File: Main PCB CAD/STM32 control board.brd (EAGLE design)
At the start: 130 x 100 mm, 113 parts, among them J1 PJ-063BH, J10 S10B-PH, J11 S10B-PH, J12 S10B-PH, J13 S10B-PH, J14 S3B-PH, J15 S3B-PH, J16 S3B-PH, J17 S3B-PH, J18 DG301-4P, J2 S4B-PH, J3 S3B-PH, J4 S3B-PH, J5 S6B-PH, J8 S6B-PH, U1 TPS7A19, U10 STM32G474, U11 DRV8701VIA, U3 L2293Q, U5 REF3330, U6 REF3318, U8 ICM_20600, X1 CSTNE

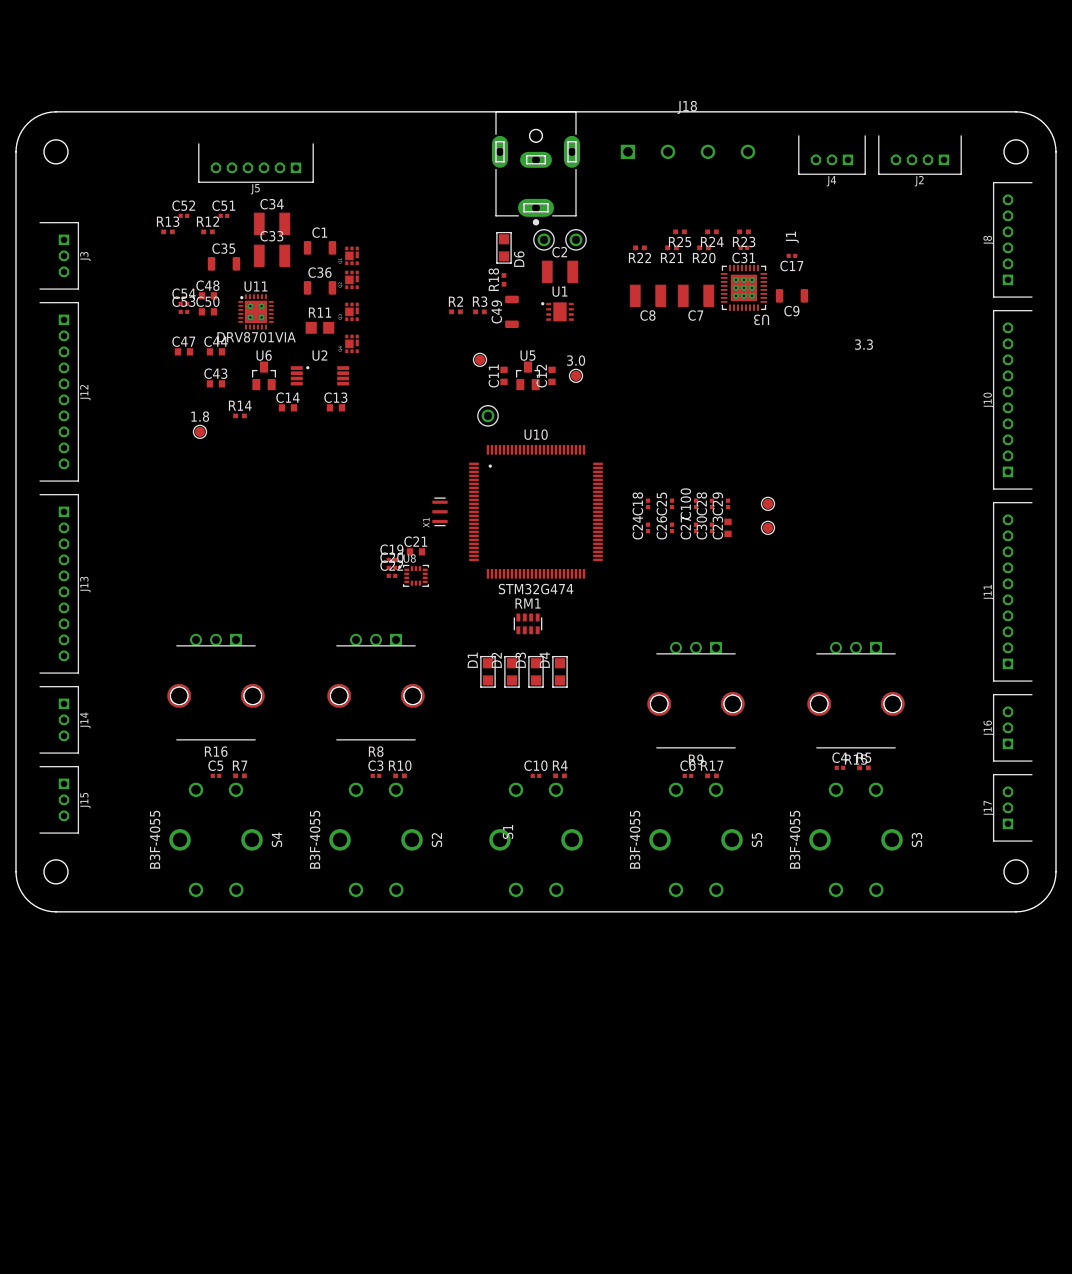
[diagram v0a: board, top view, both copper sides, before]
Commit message: renumbered schematic
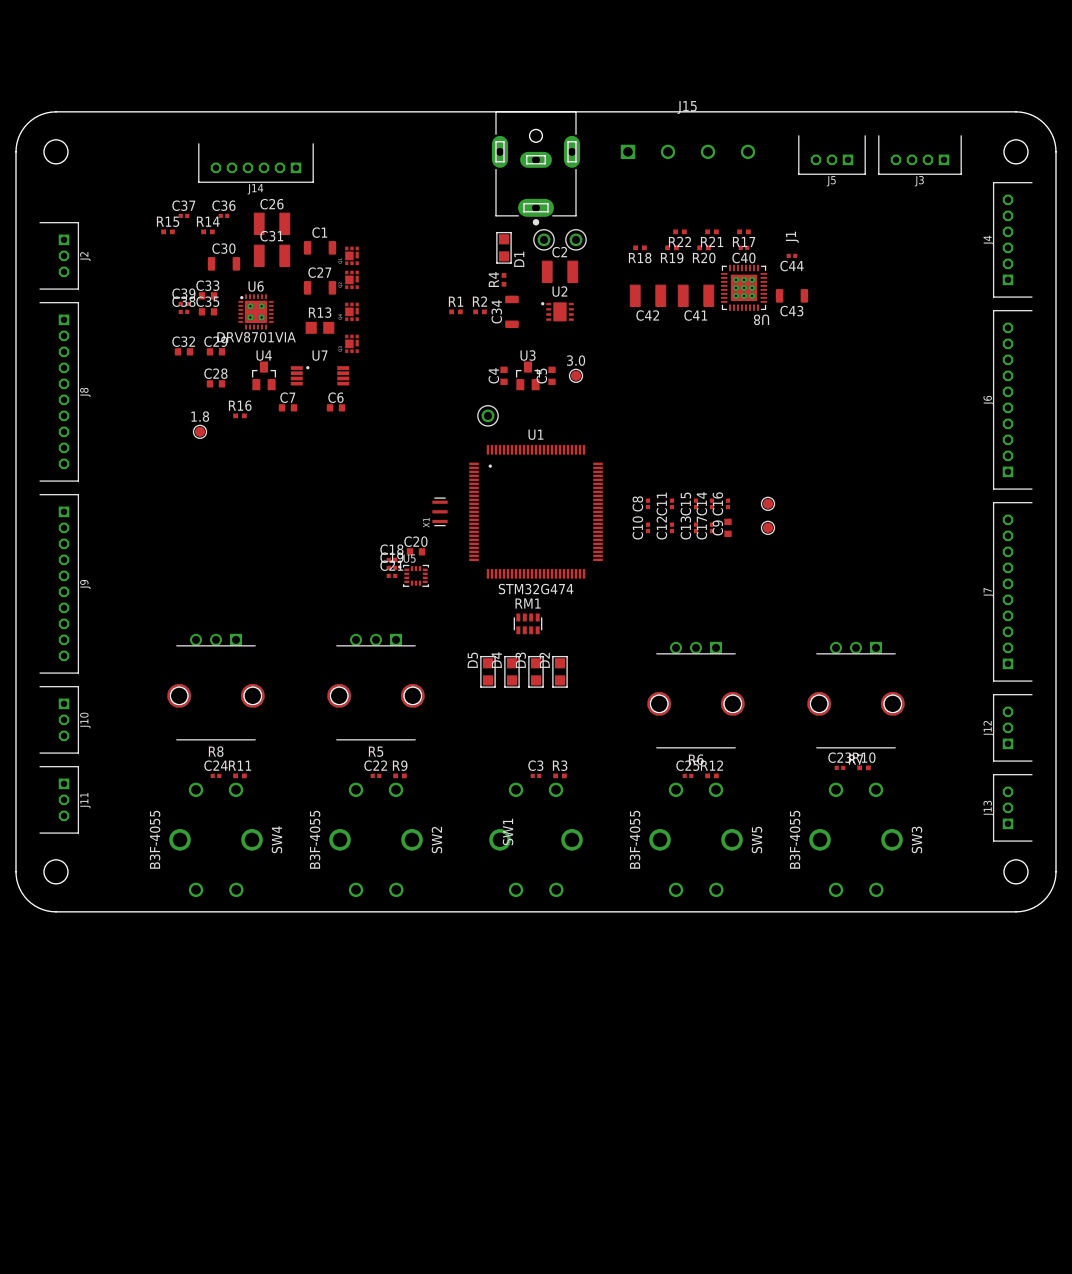
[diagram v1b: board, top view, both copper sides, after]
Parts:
- removed C48, C50: 100nF, Capacitors:C0603
- removed C49: 10uF, Capacitors:C1206
- removed C51: 1uF, Capacitors:C0402
- removed D6: Green, Semiconductor_devices:LED-0805
- removed J16, J17: S3B-PH, con-jst-ph:S3B-PH-K
- removed J18: DG301-4P, Terminal blocks:DG301-4P
- removed R23, R24, R25: 100, Resistors:R0402
- removed TP8: 3.3, testing:TP1.27MM_MASK_SILKSCREEN
- removed U10: STM32G474, stmicroelectronics:LPQFP-100
- removed U11: DRV8701VIA, Transistors drivers:VQFN-24-VIA
- added C16: 1uF, Capacitors:C0402
- added C40: 100nF, Capacitors:C0402
- added C41, C42: 47uF, Capacitors:C1210
- added D5: Blue, Semiconductor_devices:LED-0805
- added J6, J7, J9: S10B-PH, con-jst-ph:S10B-PH-K
- added R1: 16k9, Resistors:R0402
- added R19: 100, Resistors:R0402
- added R6: 10K, Resistors:ALPS_PTM
- added U4: REF3318, Voltage references:SOT-23-3
- added U7: (no value), Current sensing:TSSOP-8
- C11, C12, C13, C14, C23: value 4.7uF -> 100nF; device Capacitors:C0603 -> Capacitors:C0402
- C20, C4, C5, C6: value 100nF -> 4.7uF; device Capacitors:C0402 -> Capacitors:C0603
- C21: value 4.7uF -> 10nF; device Capacitors:C0603 -> Capacitors:C0402
- C22: value 10nF -> 100nF
- C26, C31: value 100nF -> 47uF; device Capacitors:C0402 -> Capacitors:C1210
- C27, C30: value 100nF -> 10uF; device Capacitors:C0402 -> Capacitors:C1206
- C28: device Capacitors:C0402 -> Capacitors:C0603
- C29: value 1uF -> 100nF; device Capacitors:C0402 -> Capacitors:C0603
- C33: value 47uF -> 100nF; device Capacitors:C1210 -> Capacitors:C0603
- C34: value 47uF -> 10uF; device Capacitors:C1210 -> Capacitors:C1206
- C35: value 10uF -> 100nF; device Capacitors:C1206 -> Capacitors:C0603
- C36: value 10uF -> 1uF; device Capacitors:C1206 -> Capacitors:C0402
- C43: value 100nF -> 10uF; device Capacitors:C0603 -> Capacitors:C1206
- C44: device Capacitors:C0603 -> Capacitors:C0402
- C7: value 47uF -> 4.7uF; device Capacitors:C1210 -> Capacitors:C0603
- C8: value 47uF -> 100nF; device Capacitors:C1210 -> Capacitors:C0402
- C9: value 10uF -> 4.7uF; device Capacitors:C1206 -> Capacitors:C0603
- D1: value Blue -> Green
- J10, J11, J12, J13: value S10B-PH -> S3B-PH; device con-jst-ph:S10B-PH-K -> con-jst-ph:S3B-PH-K
- J14, J4: value S3B-PH -> S6B-PH; device con-jst-ph:S3B-PH-K -> con-jst-ph:S6B-PH-K
- J15: value S3B-PH -> DG301-4P; device con-jst-ph:S3B-PH-K -> Terminal blocks:DG301-4P
- J2: value S4B-PH -> S3B-PH; device con-jst-ph:S4B-PH-K -> con-jst-ph:S3B-PH-K
- J3: value S3B-PH -> S4B-PH; device con-jst-ph:S3B-PH-K -> con-jst-ph:S4B-PH-K
- J5: value S6B-PH -> S3B-PH; device con-jst-ph:S6B-PH-K -> con-jst-ph:S3B-PH-K
- J8: value S6B-PH -> S10B-PH; device con-jst-ph:S6B-PH-K -> con-jst-ph:S10B-PH-K
- R11: value 10 mOhm -> 10k; device Resistors:CS_R0805 -> Resistors:R0402
- R13: value 10k -> 10 mOhm; device Resistors:R0402 -> Resistors:CS_R0805
- R14: value 510k -> 10k
- R15, R9: value 10K -> 10k; device Resistors:ALPS_PTM -> Resistors:R0402
- R16: value 10K -> 510k; device Resistors:ALPS_PTM -> Resistors:R0402
- R17: value 10k -> 100
- R18: value Calc_needed -> 100
- R2: value 30.9k -> 10k
- R4: value 10k -> Calc_needed
- R5, R7: value 10k -> 10K; device Resistors:R0402 -> Resistors:ALPS_PTM
- U1: value TPS7A19 -> STM32G474; device LDOs:DRB0008B -> stmicroelectronics:LPQFP-100
- U2: value (none) -> TPS7A19; device Current sensing:TSSOP-8 -> LDOs:DRB0008B
- U3: value L2293Q -> REF3330; device Transistors drivers:QFN_293Q_STM -> Voltage references:SOT-23-3
- U5: value REF3330 -> ICM_20600; device Voltage references:SOT-23-3 -> InvenSence:14_PIN_LGA
- U6: value REF3318 -> DRV8701VIA; device Voltage references:SOT-23-3 -> Transistors drivers:VQFN-24-VIA
- U8: value ICM_20600 -> L2293Q; device InvenSence:14_PIN_LGA -> Transistors drivers:QFN_293Q_STM
- moved J12 125.3 mm to (124.0, 23.0), turned to 90 degrees
- moved J10 124.6 mm to (6.00, 24.0), turned to 270 degrees
- moved J13 121.3 mm to (124.0, 13.0), turned to 90 degrees
- moved J11 120.8 mm to (6.00, 14.0), turned to 270 degrees
- moved J8 119.5 mm to (6.00, 65.0), turned to 270 degrees
- moved J15 112.4 mm to (84.0, 95.0), turned to 0 degrees
- moved J2 107.7 mm to (6.00, 82.0), turned to 270 degrees
- moved J3 107.7 mm to (113.0, 94.0), turned to 180 degrees
- moved R15 100.5 mm to (19.0, 85.0), turned to 0 degrees
- moved R12 92.7 mm to (87.0, 17.0)
- moved R7 78.6 mm to (105.0, 33.0), turned to 180 degrees
- moved J14 73.1 mm to (30.0, 93.0), turned to 180 degrees
- moved C44 73.0 mm to (97.0, 82.0), turned to 180 degrees
- moved C43 72.8 mm to (97.0, 77.0), turned to 180 degrees
- moved J5 72.0 mm to (102.0, 94.0)
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- renumbered 5V to 3V3, C100 to C15, C47 to C32, C52 to C37, C53 to C38, C54 to C39, S1 to SW1, S2 to SW2, S3 to SW3, S4 to SW4, S5 to SW5, TP6 to 1.8, TP7 to 3.0
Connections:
- net +1.8V: now also C7.1, U4.2, U7.6, U7.7; no longer C14.1, U2.6, U2.7, U6.2
- net +3V: now also C5.1, C8.1, R5.P$1, R6.P$1, R7.P$1, U1.36, U3.2; no longer C12.1, C18.1, R15.P$1, R16.P$1, R9.P$1, U10.36, U5.2
- net +3V3: now also C10.1, C12.1, C14.1, C16.1, C17.1, C19.1, C4.1, C6.1, C9.1, J14.2, J3.1, J4.1, J6.1, J7.1, J9.1, R1.2, R11.2, R12.2, R3.1, R4.2, R9.2, U1.100, U1.24, U1.37, U1.49, U1.6, U1.64, U1.75, U2.2, U3.3, U4.3, U5.5, U5.8, U7.5; no longer C22.1, C23.1, C24.1, C25.1, C26.1, C27.1, C28.1, C29.1, C30.1, J14.1, J15.1, J16.1, J17.1, J2.1, J5.2, R17.2, R18.2, R2.2, R4.1, R5.2, R7.2, TP8.1, U1.2, U10.100, U10.24, U10.37, U10.49, U10.6, U10.64, U10.75, U2.5, U5.3, U6.3, U8.5, U8.8
- net AVDD1: now also C36.2, U6.6, U6.7; no longer C51.2, U11.6, U11.7
- net BRIDGE1_EN: now also R21.1, U1.10; no longer R24.1, U10.10
- net BRIDGE2_EN: now also R22.1, U1.11; no longer R25.1, U10.11
- net DRV2_SNSOUT: now also R15.1, U6.10; no longer R13.1, U11.10
- net DVDD2: now also R14.2, R15.2, U6.8; no longer R12.2, R13.2, U11.8
- net ENCODER_1: now also J14.3, U1.91; no longer J5.3, U10.91
- net ENCODER_2: now also J14.4, U1.92; no longer J5.4, U10.92
- net FDCAN2_RX: now also U1.51; no longer U10.51
- net FDCAN2_TX: now also U1.52; no longer U10.52
- net FDCAN_STB: now also U1.73; no longer U10.73
- net GND: now also C16.2, C36.1, C40.2, C41.2, C42.2, D5.-, J10.3, J11.3, J12.3, J13.3, J14.5, J2.3, J3.4, J4.6, J5.3, J6.2, J7.2, J8.2, J9.2, R16.1, R2.1, R5.P$3, R6.P$3, R7.P$3, U1.23, U1.35, U1.48, U1.63, U1.74, U1.95, U1.99, U2.5, U2.9, U4.1, U5.6, U5.7, U6.16, U6.20, U6.21, U6.25, U6.26, U6.27, U6.28, U6.29, U6.5, U7.4, U8.1, U8.17, U8.18, U8.19, U8.2, U8.20, U8.21, U8.22, U8.23, U8.24, U8.28, U8.3, U8.32, U8.4, U8.5, U8.8, U8.9, U8.P$1, U8.P$2, U8.P$3, U8.P$4, U8.P$5, U8.P$6, U8.P$7, U8.P$8, U8.P$9, U8.PAD; no longer C33.2, C36.2, C49.2, C50.2, C51.1, D6.-, J10.2, J11.2, J12.2, J13.2, J14.3, J15.3, J16.3, J17.3, J2.4, J3.3, J4.3, J5.5, J8.6, R14.1, R15.P$3, R16.P$3, R3.1, R9.P$3, U1.4, U1.5, U1.9, U10.23, U10.35, U10.48, U10.63, U10.74, U10.95, U10.99, U11.16, U11.20, U11.21, U11.25, U11.26, U11.27, U11.28, U11.29, U11.5, U3.17, U3.18, U3.19, U3.2, U3.20, U3.21, U3.22, U3.23, U3.24, U3.28, U3.3, U3.32, U3.4, U3.5, U3.6, U3.7, U3.8, U3.9, U3.P$1, U3.P$2, U3.P$3, U3.P$4, U3.P$5, U3.P$6, U3.P$7, U3.P$8, U3.P$9, U3.PAD, U5.1, U6.1
- net I2C3_SCL: now also J5.2, U1.67; no longer J4.2, U10.67
- net I2C3_SDA: now also J5.1, U1.68; no longer J4.1, U10.68
- net ICM_CS: now also U1.26, U5.12; no longer U10.26, U8.12
- net ICM_INT1: now also U1.30, U5.4; no longer U10.30, U8.4
- net ICM_INT2: now also U1.31, U5.9; no longer U10.31, U8.9
- net ICM_MISO: now also U1.28, U5.1; no longer U10.28, U8.1
- net ICM_MOSI: now also U1.29, U5.14; no longer U10.29, U8.14
- net ICM_SCK: now also U1.27, U5.13; no longer U10.27, U8.13
- net M1: now also J14.1, R13.2, U7.2; no longer J5.1, R11.2, U2.2
- net M2: now also J14.6, Q4.D1, Q4.D2, Q4.D5, Q4.D6, Q4.D7; no longer J5.6, Q3.D1, Q3.D2, Q3.D5, Q3.D6, Q3.D7
- net MOTOR_CS: now also U1.32, U7.8; no longer U10.32, U2.8
- net M_GH1: now also U6.17; no longer U11.17
- net M_GH2: now also U6.24; no longer U11.24
- net M_GL1: now also Q3.G3, U6.19; no longer Q4.G3, U11.19
- net M_GL2: now also Q4.G3, U6.22; no longer Q3.G3, U11.22
- net M_IN1: now also U1.93, U6.15; no longer U10.93, U11.15
- net M_IN2: now also U1.94, U6.14; no longer U10.94, U11.14
- net M_NFAULT: now also R14.1, U1.96, U6.9; no longer R12.1, U10.96, U11.9
- net M_NSLEEP: now also U1.90, U6.13; no longer U10.90, U11.13
- net M_SH1: now also Q3.D1, Q3.D2, Q3.D5, Q3.D6, Q3.D7, R13.1, U6.18, U7.3; no longer Q4.D1, Q4.D2, Q4.D5, Q4.D6, Q4.D7, R11.1, U11.18, U2.3
- net M_SH2: now also U6.23; no longer U11.23
- net N$1: now also U1.12; no longer U10.12
- net N$11: now also D2.+; no longer D4.+
- net N$15: now also R18.2, U8.11; no longer R22.2, U3.11
- net N$16: now also R19.2, U8.15; no longer R21.2, U3.15
- net N$17: now also C40.1, U8.27; no longer C31.1, U3.27
- net N$18: now also U8.26; no longer U3.26
- net N$19: now also R21.2, U8.29; no longer R24.2, U3.29
- net N$2: now also U1.13; no longer U10.13
- net N$20: now also R22.2, U8.14; no longer R25.2, U3.14
- net N$21: now also R1.1, R2.2, U2.3; no longer R2.1, R3.2, U1.3
- net N$24: now also C33.1, U6.3; no longer C48.1, U11.3
- net N$32: now also C33.2, U6.4; no longer C48.2, U11.4
- net N$33: now also U6.2; no longer U11.2
- net N$37: now also R16.2, U6.12; no longer R14.2, U11.12
- net N$4: now also D5.+; no longer D1.+
- net N$5: now also D4.+; no longer D2.+
- net N$7: now also D1.+, R4.1; no longer D6.+, R18.1
- net N$8: now also R17.2, U8.30; no longer R23.2, U3.30
- net PA0: now also J10.2, U1.20; no longer J14.2, U10.20
- net PA1: now also J11.2, U1.21; no longer J15.2, U10.21
- net PA2: now also J12.2, U1.22; no longer J16.2, U10.22
- net PA3: now also J13.2, U1.25; no longer J17.2, U10.25
- net PB1: now also U1.33; no longer U10.33
- net PB14: now also C22.1, R9.1, U1.53; no longer C3.1, R10.1, U10.53
- net PB15: now also C23.1, R10.1, U1.54; no longer C4.1, R5.1, U10.54
- net PB2: now also U1.34; no longer U10.34
- net PC0: now also R5.P$2, U1.15; no longer R8.P$2, U10.15
- net PC1: now also R6.P$2, U1.16; no longer R9.P$2, U10.16
- net PC13: now also C24.1, R11.1, U1.7; no longer C5.1, R7.1, U10.7
- net PC14: now also C25.1, R12.1, U1.8; no longer C6.1, R17.1, U10.8
- net PC2: now also R7.P$2, U1.17; no longer R15.P$2, U10.17
- net PC3: now also R8.P$2, U1.18; no longer R16.P$2, U10.18
- net PC6: now also U1.65; no longer U10.65
- net PC7: now also U1.66; no longer U10.66
- net PD0: now also J6.3, U1.82; no longer J10.3, U10.82
- net PD1: now also J6.4, U1.83; no longer J10.4, U10.83
- net PD10: now also J7.5, U1.57; no longer J11.5, U10.57
- net PD11: now also J7.6, U1.58; no longer J11.6, U10.58
- net PD12: now also J7.7, U1.59; no longer J11.7, U10.59
- net PD13: now also J7.8, U1.60; no longer J11.8, U10.60
- net PD14: now also J7.9, U1.61; no longer J11.9, U10.61
- net PD15: now also J7.10, U1.62; no longer J11.10, U10.62
- net PD2: now also J6.5, U1.84; no longer J10.5, U10.84
- net PD3: now also J6.6, U1.85; no longer J10.6, U10.85
- net PD4: now also J6.7, U1.86; no longer J10.7, U10.86
- net PD5: now also J6.8, U1.87; no longer J10.8, U10.87
- net PD6: now also J6.9, U1.88; no longer J10.9, U10.88
- net PD7: now also J6.10, U1.89; no longer J10.10, U10.89
- net PD8: now also J7.3, U1.55; no longer J11.3, U10.55
- net PD9: now also J7.4, U1.56; no longer J11.4, U10.56
- net PE0: now also J8.3, U1.97; no longer J12.3, U10.97
- net PE1: now also J8.4, U1.98; no longer J12.4, U10.98
- net PE10: now also J9.5, U1.41; no longer J13.5, U10.41
- net PE11: now also J9.6, U1.42; no longer J13.6, U10.42
- net PE12: now also J9.7, U1.43; no longer J13.7, U10.43
- net PE13: now also J9.8, U1.44; no longer J13.8, U10.44
- net PE14: now also J9.9, U1.45; no longer J13.9, U10.45
- net PE15: now also J9.10, U1.46; no longer J13.10, U10.46
- net PE2: now also J8.5, U1.1; no longer J12.5, U10.1
- net PE3: now also J8.6, U1.2; no longer J12.6, U10.2
- net PE4: now also J8.7, U1.3; no longer J12.7, U10.3
- net PE5: now also J8.8, U1.4; no longer J12.8, U10.4
- net PE6: now also J8.9, U1.5; no longer J12.9, U10.5
- net PE7: now also J8.10, U1.38; no longer J12.10, U10.38
- net PE8: now also J9.3, U1.39; no longer J13.3, U10.39
- net PE9: now also J9.4, U1.40; no longer J13.4, U10.40
- net POUT1: now also J15.1, U8.31; no longer J18.1, U3.31
- net POUT2: now also J15.2, U8.10; no longer J18.2, U3.10
- net POUT3: now also J15.3, U8.16; no longer J18.3, U3.16
- net POUT4: now also J15.4, U8.25; no longer J18.4, U3.25
- net POWER_OUT1: now also R17.1, U1.69; no longer R23.1, U10.69
- net POWER_OUT2: now also R18.1, U1.70; no longer R22.1, U10.70
- net POWER_OUT3: now also R19.1, U1.71; no longer R21.1, U10.71
- net POWER_OUT4: now also U1.72; no longer U10.72
- net REG: now also C18.1, U5.11; no longer C19.1, U8.11
- net RST: now also C3.1, R3.2, U1.14; no longer C10.1, R4.2, U10.14
- net SPI3_MISO: now also J4.3, U1.80; no longer J8.3, U10.80
- net SPI3_MOSI: now also J4.2, U1.81; no longer J8.2, U10.81
- net SPI3_SCK: now also J4.4, U1.79; no longer J8.4, U10.79
- net SPI_CS: now also J4.5, U1.78; no longer J8.5, U10.78
- net SWCLK: now also J3.3, U1.77; no longer J2.3, U10.77
- net SWDIO: now also J3.2, U1.76; no longer J2.2, U10.76
- net USART3_RX: now also J2.2, U1.50; no longer J3.2, U10.50
- net USART3_TX: now also J2.1, U1.47; no longer J3.1, U10.47
- net VDD: now also C26.1, C27.1, C28.1, C29.1, C30.1, C31.1, C41.1, C42.1, U2.6, U2.7, U6.1, U8.12, U8.13; no longer C17.1, C33.1, C36.1, C49.1, C50.1, C7.1, C8.1, C9.1, U1.6, U1.7, U11.1, U3.12, U3.13

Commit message: Can removed
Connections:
- removed net FDCAN2_RX: U1.51
- removed net FDCAN2_TX: U1.52
- removed net FDCAN_STB: U1.73
- removed net M2: J14.6, Q2.S4, Q2.S8, Q4.D1, Q4.D2, Q4.D5, Q4.D6, Q4.D7
- net M_SH2: now also J14.6, Q2.S4, Q2.S8, Q4.D1, Q4.D2, Q4.D5, Q4.D6, Q4.D7

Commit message: for BOM review
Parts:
- added C45, C46, C47, C48: 22uF, Capacitors:C1210
- added C49: 10uF, Capacitors:C1206
- added C50: 100nF, Capacitors:C0402
- C11, C22, C8: value 100nF -> 4.7uF; device Capacitors:C0402 -> Capacitors:C0603
- C16, C37: value 1uF -> 100nF
- C18, C40: value 100nF -> 1uF; device Capacitors:C0402 -> Capacitors:C0603
- C2: value 47uF -> 22uF
- C20, C5: value 4.7uF -> 100nF; device Capacitors:C0603 -> Capacitors:C0402
- C21: value 10nF -> 100nF
- C23: value 100nF -> 10nF
- C26, C31, C42: value 47uF -> 100nF; device Capacitors:C1210 -> Capacitors:C0402
- C27, C43: value 10uF -> 100nF; device Capacitors:C1206 -> Capacitors:C0402
- C28, C29, C35: value 100nF -> 22uF; device Capacitors:C0603 -> Capacitors:C1210
- C3: value 100nF -> 22uF; device Capacitors:C0402 -> Capacitors:C1210
- C32: value 1uF -> 100nF; device Capacitors:C0603 -> Capacitors:C0402
- C33: value 100nF -> 10uF; device Capacitors:C0603 -> Capacitors:C1206
- C34: value 10uF -> 22uF; device Capacitors:C1206 -> Capacitors:C1210
- C36: device Capacitors:C0402 -> Capacitors:C0603
- C38: value 100nF -> 10uF; device Capacitors:C0402 -> Capacitors:C1206
- C4: value 4.7uF -> 10uF; device Capacitors:C0603 -> Capacitors:C1206
- C41: value 47uF -> 1uF; device Capacitors:C1210 -> Capacitors:C0603
- R4: value Calc_needed -> 10k
- RM1: value RES_ARRAY -> RES_ARRAY0402_YAGEO; device Resistors:0603-ARC -> Resistors:0402-ARC
- moved C35 103.4 mm to (5.08, -26.7)
- moved C4 97.8 mm to (2.54, -11.4), turned to 0 degrees
- moved C28 87.4 mm to (5.08, -19.1)
- moved C27 76.4 mm to (84.0, 17.0)
- moved C43 76.0 mm to (21.0, 76.0), turned to 0 degrees
- moved C26 69.4 mm to (25.0, 17.0)
- moved C40 65.1 mm to (26.0, 87.0), turned to 0 degrees
- moved C41 64.8 mm to (21.0, 87.0), turned to 0 degrees
- moved C3 64.6 mm to (3.81, -3.81)
- moved C23 60.9 mm to (47.0, 42.0)
- moved C42 58.0 mm to (21.0, 75.0), turned to 0 degrees
- moved C9 57.0 mm to (34.0, 63.0), turned to 0 degrees
- moved C5 50.0 mm to (65.0, 17.0), turned to 0 degrees
- moved C18 42.6 mm to (89.0, 51.0), turned to 90 degrees
- moved C38 41.0 mm to (62.0, 75.0), turned to 90 degrees
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- renumbered 1.8 to TP5, 3.0 to TP4, 3V3 to TP1, GND to TP3, VIN to TP2
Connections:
- net +1.8V: now also C42.1, C9.1; no longer C38.1, C7.1
- net +3V: now also C10.1, C7.1; no longer C5.1, C8.1
- net +3V3: now also C18.1, C22.1, C23.1, C3.1, C43.1, C8.1; no longer C10.1, C20.1, C39.1, C9.1
- net AVDD1: now also C40.2; no longer C36.2
- net DVDD2: now also C41.2; no longer C37.2
- net GND: now also C32.2, C33.2, C40.1, C41.1, C45.2, C46.2, C47.2, C48.2, C49.2, C50.2; no longer C36.1, C37.1, C40.2, C41.2
- net N$11: now also RM1.11; no longer RM1.8
- net N$17: now also C44.1; no longer C40.1
- net N$24: now also C37.1; no longer C33.1
- net N$32: now also C37.2; no longer C33.2
- net N$33: now also C36.2; no longer C32.2
- net N$4: now also RM1.44; no longer RM1.5
- net N$5: now also RM1.33; no longer RM1.6
- net N$6: now also RM1.22; no longer RM1.7
- net PB14: now also C24.1; no longer C22.1
- net PB15: now also C25.1; no longer C23.1
- net PC13: now also C26.1; no longer C24.1
- net PC14: now also C27.1; no longer C25.1
- net REG: now also C20.1; no longer C18.1
- net RST: now also C5.1; no longer C3.1
- net VDD: now also C33.1, C36.1, C38.1, C39.1, C45.1, C46.1, C47.1, C48.1, C49.1, C50.1; no longer C26.1, C27.1, C41.1, C42.1, C43.1, C44.1
